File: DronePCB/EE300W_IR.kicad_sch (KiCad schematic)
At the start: 18 parts, among them Q1 AO3400A, Q2 AO3400A, U2 TSOP45xx

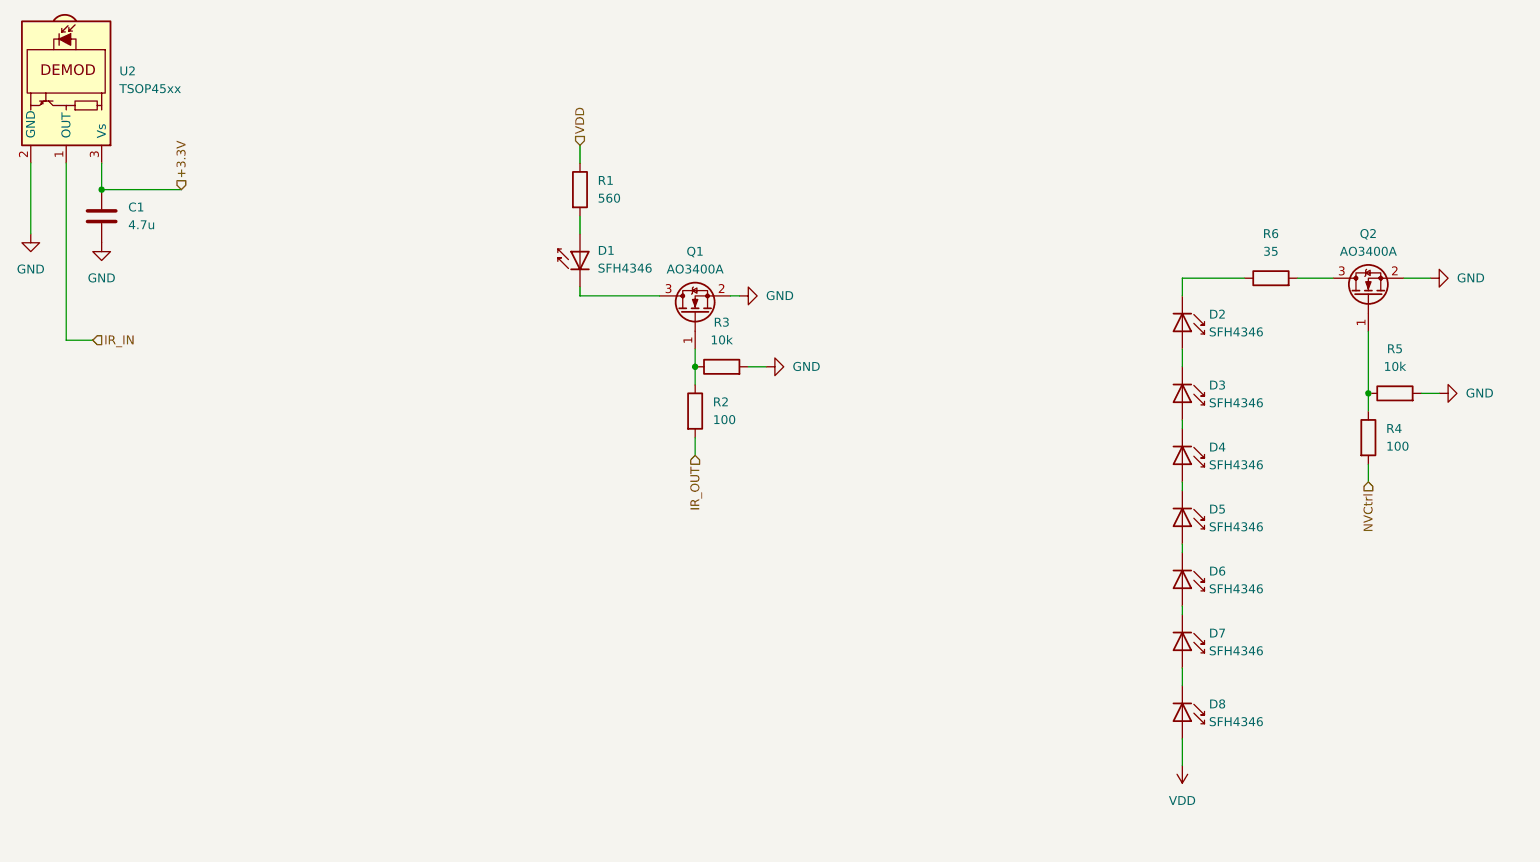
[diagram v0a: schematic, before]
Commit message: Added IR circuit to main schematic | fixed RPi header gnd
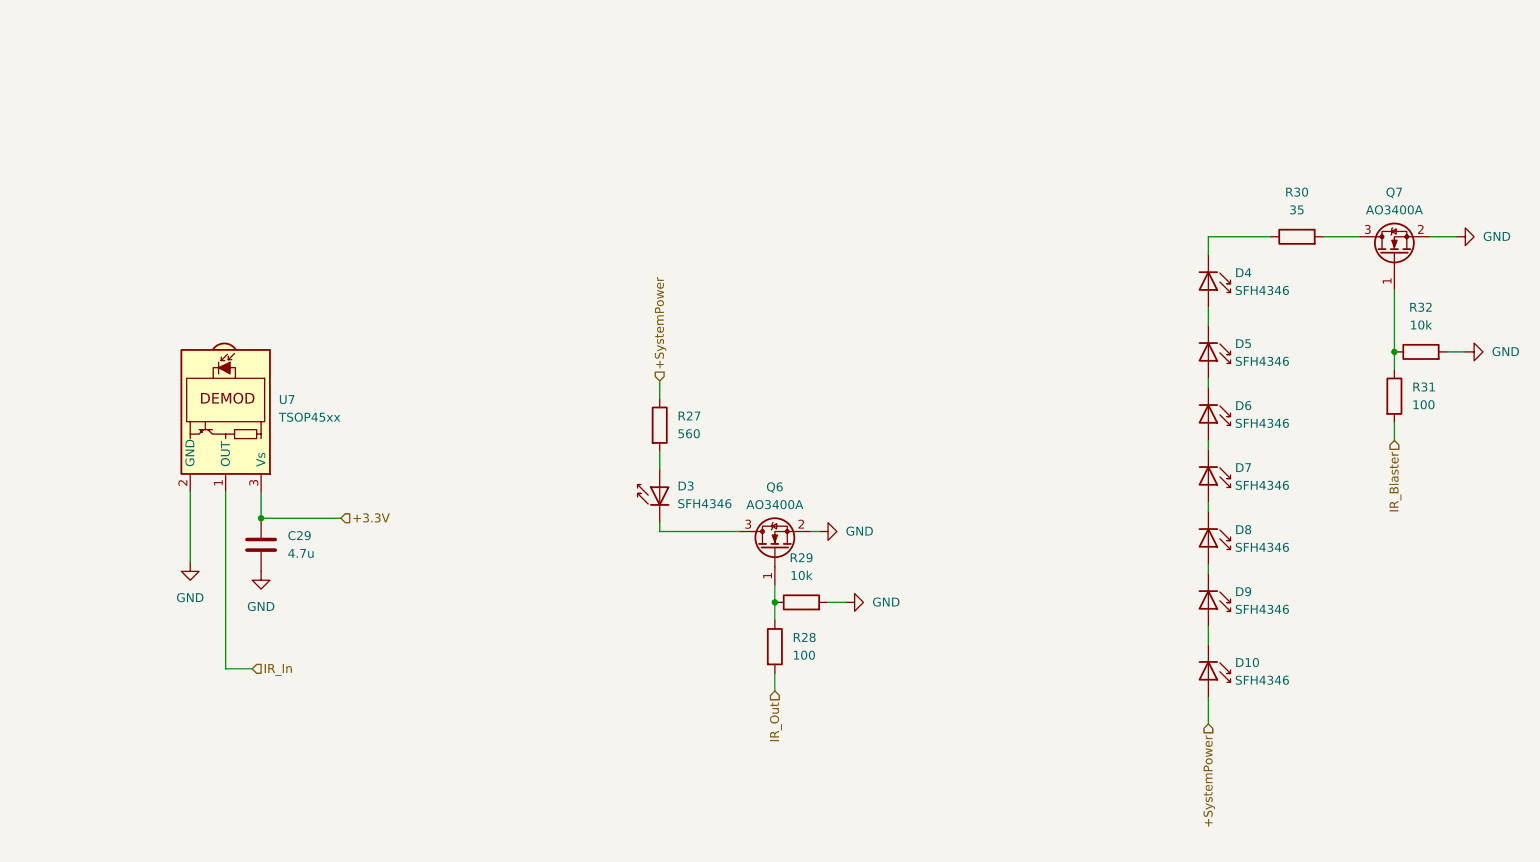
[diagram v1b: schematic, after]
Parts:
- renumbered C1 to C29, D8 to D10, D1 to D3, D2 to D4, D3 to D5, D4 to D6, D5 to D7, D6 to D8, D7 to D9, Q1 to Q6, Q2 to Q7, R1 to R27, R2 to R28, R3 to R29, R6 to R30, R4 to R31, R5 to R32, U2 to U7
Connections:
- net IR_IN renamed IR_In
- net IR_OUT renamed IR_Out
- net NVCtrl renamed IR_Blaster
- net VDD renamed +SystemPower
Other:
- moved on the sheet: C29, D10, D3, D4, D5, D6, D7, D8, D9, Q6, Q7, R27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

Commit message: Completed H-Bridge Circuit | Finished Schematic | Working on pcb design
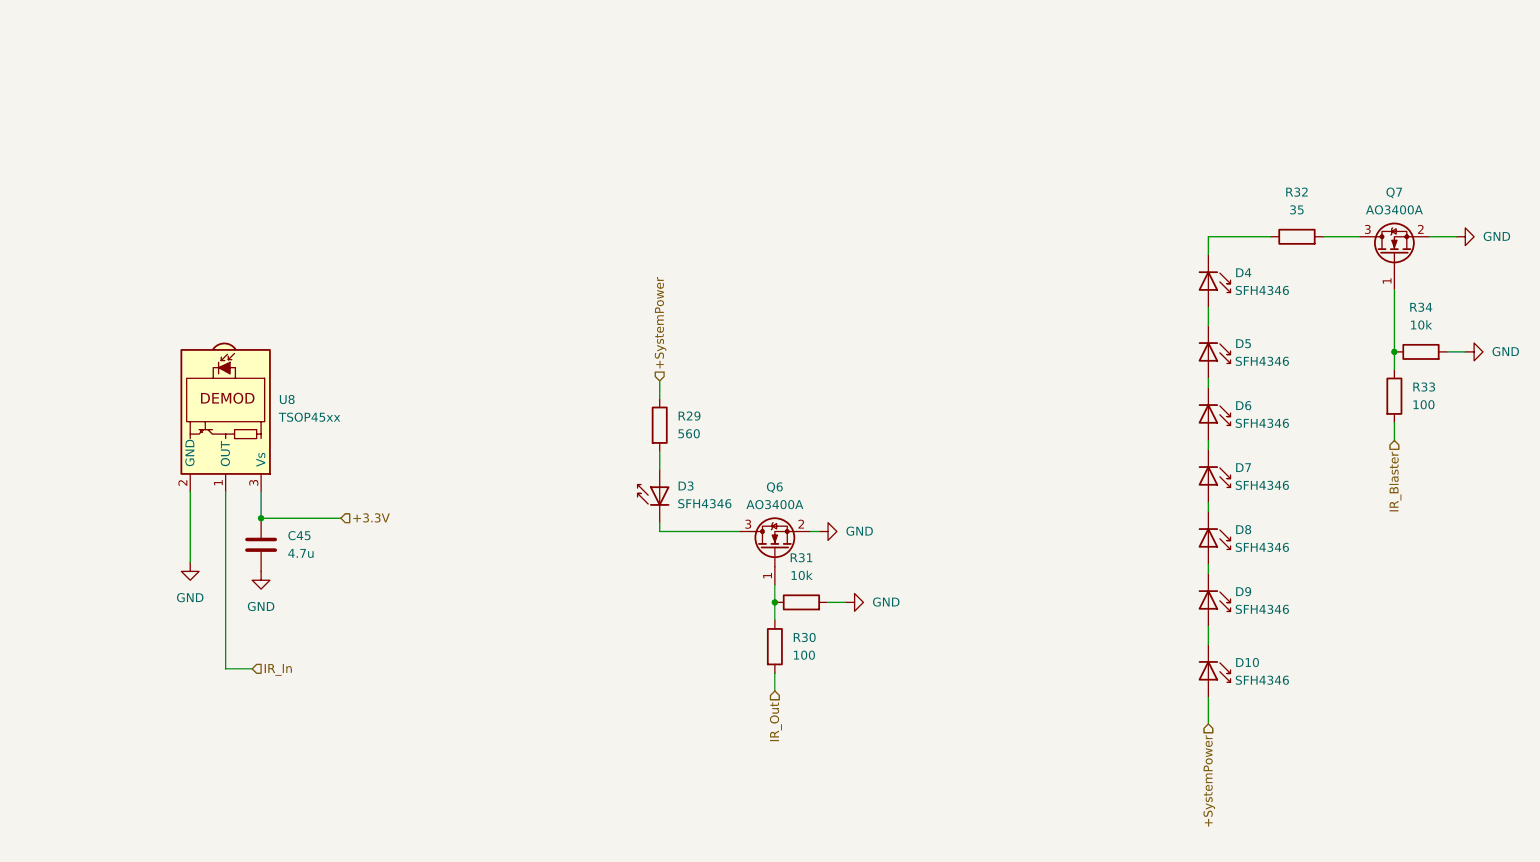
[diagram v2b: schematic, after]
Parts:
- C45: renamed from C29; footprint (none) -> Capacitor_SMD:C_0603_1608Metric
- R29: renamed from R27; footprint (none) -> Resistor_SMD:R_0603_1608Metric
- R30: renamed from R28; footprint (none) -> Resistor_SMD:R_0603_1608Metric
- R31: renamed from R29; footprint (none) -> Resistor_SMD:R_0603_1608Metric
- R32: renamed from R30; footprint (none) -> Resistor_SMD:R_0603_1608Metric
- R33: renamed from R31; footprint (none) -> Resistor_SMD:R_0603_1608Metric
- R34: renamed from R32; footprint (none) -> Resistor_SMD:R_0603_1608Metric
- renumbered U7 to U8
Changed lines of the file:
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@@
 		(dnp no)
 		(fields_autoplaced yes)
-		(property "Reference" "R28"
+		(property "Reference" "R30"
 			(at 146.05 115.0559 0)
 			(show_name no)
@@
 			)
 		)
-		(property "Footprint" ""
+		(property "Footprint" "Resistor_SMD:R_0603_1608Metric"
 			(at 141.732 116.326 90)
 			(hide yes)
@@
 			(project "DronePCB"
 				(path "/c9b74494-ac48-4f27-9459-39f0e04d9d05/3ee54b6d-b171-4c99-9842-f11b3399863d"
-					(reference "R28")
+					(reference "R30")
 					(unit 1)
 				)
@@
 		(dnp no)
 		(fields_autoplaced yes)
-		(property "Reference" "#PWR05"
+		(property "Reference" "#PWR061"
 			(at 160.02 109.976 0)
 			(hide yes)
@@
 			(project "DronePCB"
 				(path "/c9b74494-ac48-4f27-9459-39f0e04d9d05/3ee54b6d-b171-4c99-9842-f11b3399863d"
-					(reference "#PWR05")
+					(reference "#PWR061")
 					(unit 1)
 				)
@@
 		(dnp no)
 		(fields_autoplaced yes)
-		(property "Reference" "R32"
+		(property "Reference" "R34"
 			(at 236.1421 67.7177 90)
 			(show_name no)
@@
 			)
 		)
-		(property "Footprint" ""
+		(property "Footprint" "Resistor_SMD:R_0603_1608Metric"
 			(at 236.1421 75.8457 90)
 			(hide yes)
@@
 			(project "DronePCB"
 				(path "/c9b74494-ac48-4f27-9459-39f0e04d9d05/3ee54b6d-b171-4c99-9842-f11b3399863d"
-					(reference "R32")
+					(reference "R34")
 					(unit 1)
 				)
@@
 		(dnp no)
 		(fields_autoplaced yes)
-		(property "Reference" "#PWR02"
+		(property "Reference" "#PWR059"
 			(at 69.85 111.8836 0)
 			(hide yes)
@@
 			(project "DronePCB"
 				(path "/c9b74494-ac48-4f27-9459-39f0e04d9d05/3ee54b6d-b171-4c99-9842-f11b3399863d"
-					(reference "#PWR02")
+					(reference "#PWR059")
 					(unit 1)
 				)
@@
 		(dnp no)
 		(fields_autoplaced yes)
-		(property "Reference" "R31"
+		(property "Reference" "R33"
 			(at 234.8721 79.1476 0)
 			(show_name no)
@@
 			)
 		)
-		(property "Footprint" ""
+		(property "Footprint" "Resistor_SMD:R_0603_1608Metric"
 			(at 230.5541 80.4177 90)
 			(hide yes)
@@
 			(project "DronePCB"
 				(path "/c9b74494-ac48-4f27-9459-39f0e04d9d05/3ee54b6d-b171-4c99-9842-f11b3399863d"
-					(reference "R31")
+					(reference "R33")
 					(unit 1)
 				)
@@
 		(dnp no)
 		(fields_autoplaced yes)
-		(property "Reference" "#PWR06"
+		(property "Reference" "#PWR060"
 			(at 156.21 99.816 0)
 			(hide yes)
@@
 			(project "DronePCB"
 				(path "/c9b74494-ac48-4f27-9459-39f0e04d9d05/3ee54b6d-b171-4c99-9842-f11b3399863d"
-					(reference "#PWR06")
+					(reference "#PWR060")
 					(unit 1)
 				)
@@
 		(dnp no)
 		(fields_autoplaced yes)
-		(property "Reference" "C29"
+		(property "Reference" "C45"
 			(at 73.66 100.4535 0)
 			(show_name no)
@@
 			)
 		)
-		(property "Footprint" ""
+		(property "Footprint" "Capacitor_SMD:C_0603_1608Metric"
 			(at 70.8152 105.5336 0)
 			(hide yes)
@@
 			(project "DronePCB"
 				(path "/c9b74494-ac48-4f27-9459-39f0e04d9d05/3ee54b6d-b171-4c99-9842-f11b3399863d"
-					(reference "C29")
+					(reference "C45")
 					(unit 1)
 				)
@@
 		(dnp no)
 		(fields_autoplaced yes)
-		(property "Reference" "R27"
+		(property "Reference" "R29"
 			(at 129.54 83.3059 0)
 			(show_name no)
@@
 			)
 		)
-		(property "Footprint" ""
+		(property "Footprint" "Resistor_SMD:R_0603_1608Metric"
 			(at 125.222 84.576 90)
 			(hide yes)
@@
 			(project "DronePCB"
 				(path "/c9b74494-ac48-4f27-9459-39f0e04d9d05/3ee54b6d-b171-4c99-9842-f11b3399863d"
-					(reference "R27")
+					(reference "R29")
 					(unit 1)
 				)
@@
 		(dnp no)
 		(fields_autoplaced yes)
-		(property "Reference" "#PWR07"
+		(property "Reference" "#PWR063"
 			(at 248.8421 74.0677 0)
 			(hide yes)
@@
 			(project "DronePCB"
 				(path "/c9b74494-ac48-4f27-9459-39f0e04d9d05/3ee54b6d-b171-4c99-9842-f11b3399863d"
-					(reference "#PWR07")
+					(reference "#PWR063")
 					(unit 1)
 				)
@@
 		(dnp no)
 		(fields_autoplaced yes)
-		(property "Reference" "#PWR08"
+		(property "Reference" "#PWR062"
 			(at 247.5721 57.5577 0)
 			(hide yes)
@@
 			(project "DronePCB"
 				(path "/c9b74494-ac48-4f27-9459-39f0e04d9d05/3ee54b6d-b171-4c99-9842-f11b3399863d"
-					(reference "#PWR08")
+					(reference "#PWR062")
 					(unit 1)
 				)
@@
 		(dnp no)
 		(fields_autoplaced yes)
-		(property "Reference" "#PWR01"
+		(property "Reference" "#PWR058"
 			(at 59.69 110.6136 0)
 			(hide yes)
@@
 			(project "DronePCB"
 				(path "/c9b74494-ac48-4f27-9459-39f0e04d9d05/3ee54b6d-b171-4c99-9842-f11b3399863d"
-					(reference "#PWR01")
+					(reference "#PWR058")
 					(unit 1)
 				)
@@
 		(dnp no)
 		(fields_autoplaced yes)
-		(property "Reference" "R29"
+		(property "Reference" "R31"
 			(at 147.32 103.626 90)
 			(show_name no)
@@
 			)
 		)
-		(property "Footprint" ""
+		(property "Footprint" "Resistor_SMD:R_0603_1608Metric"
 			(at 147.32 111.754 90)
 			(hide yes)
@@
 			(project "DronePCB"
 				(path "/c9b74494-ac48-4f27-9459-39f0e04d9d05/3ee54b6d-b171-4c99-9842-f11b3399863d"
-					(reference "R29")
+					(reference "R31")
 					(unit 1)
 				)
@@
 		(dnp no)
 		(fields_autoplaced yes)
-		(property "Reference" "R30"
+		(property "Reference" "R32"
 			(at 218.3621 51.2077 90)
 			(show_name no)
@@
 			)
 		)
-		(property "Footprint" ""
+		(property "Footprint" "Resistor_SMD:R_0603_1608Metric"
 			(at 218.3621 59.3357 90)
 			(hide yes)
@@
 			(project "DronePCB"
 				(path "/c9b74494-ac48-4f27-9459-39f0e04d9d05/3ee54b6d-b171-4c99-9842-f11b3399863d"
-					(reference "R30")
+					(reference "R32")
 					(unit 1)
 				)
@@
 		(dnp no)
 		(fields_autoplaced yes)
-		(property "Reference" "U7"
+		(property "Reference" "U8"
 			(at 72.39 80.9385 90)
 			(show_name no)
@@
 			(project "DronePCB"
 				(path "/c9b74494-ac48-4f27-9459-39f0e04d9d05/3ee54b6d-b171-4c99-9842-f11b3399863d"
-					(reference "U7")
-					(unit 1)
-				)
+					(reference "U8")
+					(unit 1)
+				)

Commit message: All circuits complete
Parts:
- renumbered C45 to C49, Q6 to Q4, Q7 to Q5, R29 to R30, R30 to R31, R31 to R32, R32 to R33, R33 to R34, R34 to R35
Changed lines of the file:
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@@
 		(dnp no)
 		(fields_autoplaced yes)
-		(property "Reference" "R30"
+		(property "Reference" "R31"
 			(at 146.05 115.0559 0)
 			(show_name no)
@@
 			(project "DronePCB"
 				(path "/c9b74494-ac48-4f27-9459-39f0e04d9d05/3ee54b6d-b171-4c99-9842-f11b3399863d"
-					(reference "R30")
+					(reference "R31")
 					(unit 1)
 				)
@@
 		(dnp no)
 		(fields_autoplaced yes)
-		(property "Reference" "#PWR061"
+		(property "Reference" "#PWR063"
 			(at 160.02 109.976 0)
 			(hide yes)
@@
 			(project "DronePCB"
 				(path "/c9b74494-ac48-4f27-9459-39f0e04d9d05/3ee54b6d-b171-4c99-9842-f11b3399863d"
-					(reference "#PWR061")
+					(reference "#PWR063")
 					(unit 1)
 				)
@@
 		(dnp no)
 		(fields_autoplaced yes)
-		(property "Reference" "Q7"
+		(property "Reference" "Q5"
 			(at 232.3321 51.2077 90)
 			(show_name no)
@@
 			(project "DronePCB"
 				(path "/c9b74494-ac48-4f27-9459-39f0e04d9d05/3ee54b6d-b171-4c99-9842-f11b3399863d"
-					(reference "Q7")
+					(reference "Q5")
 					(unit 1)
 				)
@@
 		(dnp no)
 		(fields_autoplaced yes)
-		(property "Reference" "R34"
+		(property "Reference" "R35"
 			(at 236.1421 67.7177 90)
 			(show_name no)
@@
 			(project "DronePCB"
 				(path "/c9b74494-ac48-4f27-9459-39f0e04d9d05/3ee54b6d-b171-4c99-9842-f11b3399863d"
-					(reference "R34")
+					(reference "R35")
 					(unit 1)
 				)
@@
 		(dnp no)
 		(fields_autoplaced yes)
-		(property "Reference" "#PWR059"
+		(property "Reference" "#PWR061"
 			(at 69.85 111.8836 0)
 			(hide yes)
@@
 			(project "DronePCB"
 				(path "/c9b74494-ac48-4f27-9459-39f0e04d9d05/3ee54b6d-b171-4c99-9842-f11b3399863d"
-					(reference "#PWR059")
+					(reference "#PWR061")
 					(unit 1)
 				)
@@
 		(dnp no)
 		(fields_autoplaced yes)
-		(property "Reference" "R33"
+		(property "Reference" "R34"
 			(at 234.8721 79.1476 0)
 			(show_name no)
@@
 			(project "DronePCB"
 				(path "/c9b74494-ac48-4f27-9459-39f0e04d9d05/3ee54b6d-b171-4c99-9842-f11b3399863d"
-					(reference "R33")
+					(reference "R34")
 					(unit 1)
 				)
@@
 		(dnp no)
 		(fields_autoplaced yes)
-		(property "Reference" "#PWR060"
+		(property "Reference" "#PWR062"
 			(at 156.21 99.816 0)
 			(hide yes)
@@
 			(project "DronePCB"
 				(path "/c9b74494-ac48-4f27-9459-39f0e04d9d05/3ee54b6d-b171-4c99-9842-f11b3399863d"
-					(reference "#PWR060")
+					(reference "#PWR062")
 					(unit 1)
 				)
@@
 		(dnp no)
 		(fields_autoplaced yes)
-		(property "Reference" "C45"
+		(property "Reference" "C49"
 			(at 73.66 100.4535 0)
 			(show_name no)
@@
 			(project "DronePCB"
 				(path "/c9b74494-ac48-4f27-9459-39f0e04d9d05/3ee54b6d-b171-4c99-9842-f11b3399863d"
-					(reference "C45")
+					(reference "C49")
 					(unit 1)
 				)
@@
 		(dnp no)
 		(fields_autoplaced yes)
-		(property "Reference" "R29"
+		(property "Reference" "R30"
 			(at 129.54 83.3059 0)
 			(show_name no)
@@
 			(project "DronePCB"
 				(path "/c9b74494-ac48-4f27-9459-39f0e04d9d05/3ee54b6d-b171-4c99-9842-f11b3399863d"
-					(reference "R29")
+					(reference "R30")
 					(unit 1)
 				)
@@
 		(dnp no)
 		(fields_autoplaced yes)
-		(property "Reference" "#PWR063"
+		(property "Reference" "#PWR065"
 			(at 248.8421 74.0677 0)
 			(hide yes)
@@
 			(project "DronePCB"
 				(path "/c9b74494-ac48-4f27-9459-39f0e04d9d05/3ee54b6d-b171-4c99-9842-f11b3399863d"
-					(reference "#PWR063")
+					(reference "#PWR065")
 					(unit 1)
 				)
@@
 		(dnp no)
 		(fields_autoplaced yes)
-		(property "Reference" "Q6"
+		(property "Reference" "Q4"
 			(at 143.51 93.466 90)
 			(show_name no)
@@
 			(project "DronePCB"
 				(path "/c9b74494-ac48-4f27-9459-39f0e04d9d05/3ee54b6d-b171-4c99-9842-f11b3399863d"
-					(reference "Q6")
+					(reference "Q4")
 					(unit 1)
 				)
@@
 		(dnp no)
 		(fields_autoplaced yes)
-		(property "Reference" "#PWR062"
+		(property "Reference" "#PWR064"
 			(at 247.5721 57.5577 0)
 			(hide yes)
@@
 			(project "DronePCB"
 				(path "/c9b74494-ac48-4f27-9459-39f0e04d9d05/3ee54b6d-b171-4c99-9842-f11b3399863d"
-					(reference "#PWR062")
+					(reference "#PWR064")
 					(unit 1)
 				)
@@
 		(dnp no)
 		(fields_autoplaced yes)
-		(property "Reference" "#PWR058"
+		(property "Reference" "#PWR060"
 			(at 59.69 110.6136 0)
 			(hide yes)
@@
 			(project "DronePCB"
 				(path "/c9b74494-ac48-4f27-9459-39f0e04d9d05/3ee54b6d-b171-4c99-9842-f11b3399863d"
-					(reference "#PWR058")
+					(reference "#PWR060")
 					(unit 1)
 				)
@@
 		(dnp no)
 		(fields_autoplaced yes)
-		(property "Reference" "R31"
+		(property "Reference" "R32"
 			(at 147.32 103.626 90)
 			(show_name no)
@@
 			(project "DronePCB"
 				(path "/c9b74494-ac48-4f27-9459-39f0e04d9d05/3ee54b6d-b171-4c99-9842-f11b3399863d"
-					(reference "R31")
+					(reference "R32")
 					(unit 1)
 				)
@@
 		(dnp no)
 		(fields_autoplaced yes)
-		(property "Reference" "R32"
+		(property "Reference" "R33"
 			(at 218.3621 51.2077 90)
 			(show_name no)
@@
 			(project "DronePCB"
 				(path "/c9b74494-ac48-4f27-9459-39f0e04d9d05/3ee54b6d-b171-4c99-9842-f11b3399863d"
-					(reference "R32")
-					(unit 1)
-				)
+					(reference "R33")
+					(unit 1)
+				)

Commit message: Rough board placement complete
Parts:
- D10, D3, D4, D5, D6, D7, D8, D9: footprint LED_THT:LED_D3.0mm_IRBlack -> LED_THT:LED_D5.0mm_IRGrey
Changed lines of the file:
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@@
 			)
 		)
-		(property "Footprint" "LED_THT:LED_D3.0mm_IRBlack"
+		(property "Footprint" "LED_THT:LED_D5.0mm_IRGrey"
 			(at 210.1071 84.2277 0)
 			(hide yes)
@@
 			)
 		)
-		(property "Footprint" "LED_THT:LED_D3.0mm_IRBlack"
+		(property "Footprint" "LED_THT:LED_D5.0mm_IRGrey"
 			(at 210.1071 110.8977 0)
 			(hide yes)
@@
 			)
 		)
-		(property "Footprint" "LED_THT:LED_D3.0mm_IRBlack"
+		(property "Footprint" "LED_THT:LED_D5.0mm_IRGrey"
 			(at 210.1071 75.3377 0)
 			(hide yes)
@@
 			)
 		)
-		(property "Footprint" "LED_THT:LED_D3.0mm_IRBlack"
+		(property "Footprint" "LED_THT:LED_D5.0mm_IRGrey"
 			(at 122.555 93.466 0)
 			(hide yes)
@@
 			)
 		)
-		(property "Footprint" "LED_THT:LED_D3.0mm_IRBlack"
+		(property "Footprint" "LED_THT:LED_D5.0mm_IRGrey"
 			(at 210.1071 102.0077 0)
 			(hide yes)
@@
 			)
 		)
-		(property "Footprint" "LED_THT:LED_D3.0mm_IRBlack"
+		(property "Footprint" "LED_THT:LED_D5.0mm_IRGrey"
 			(at 210.1071 121.0577 0)
 			(hide yes)
@@
 			)
 		)
-		(property "Footprint" "LED_THT:LED_D3.0mm_IRBlack"
+		(property "Footprint" "LED_THT:LED_D5.0mm_IRGrey"
 			(at 210.1071 65.1777 0)
 			(hide yes)
@@
 			)
 		)
-		(property "Footprint" "LED_THT:LED_D3.0mm_IRBlack"
+		(property "Footprint" "LED_THT:LED_D5.0mm_IRGrey"
 			(at 210.1071 93.1177 0)
 			(hide yes)
